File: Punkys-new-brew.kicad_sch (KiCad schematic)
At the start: 64 parts, among them J1 +12v, J10 VCA-CV, J11 1x10_main, J12 1x10_control, J13 L_1x12_main, J14 L_1x12_control, J15 R_1x12_control, J16 R_1x12_main, J17 ScrewHole, J18 ScrewHole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

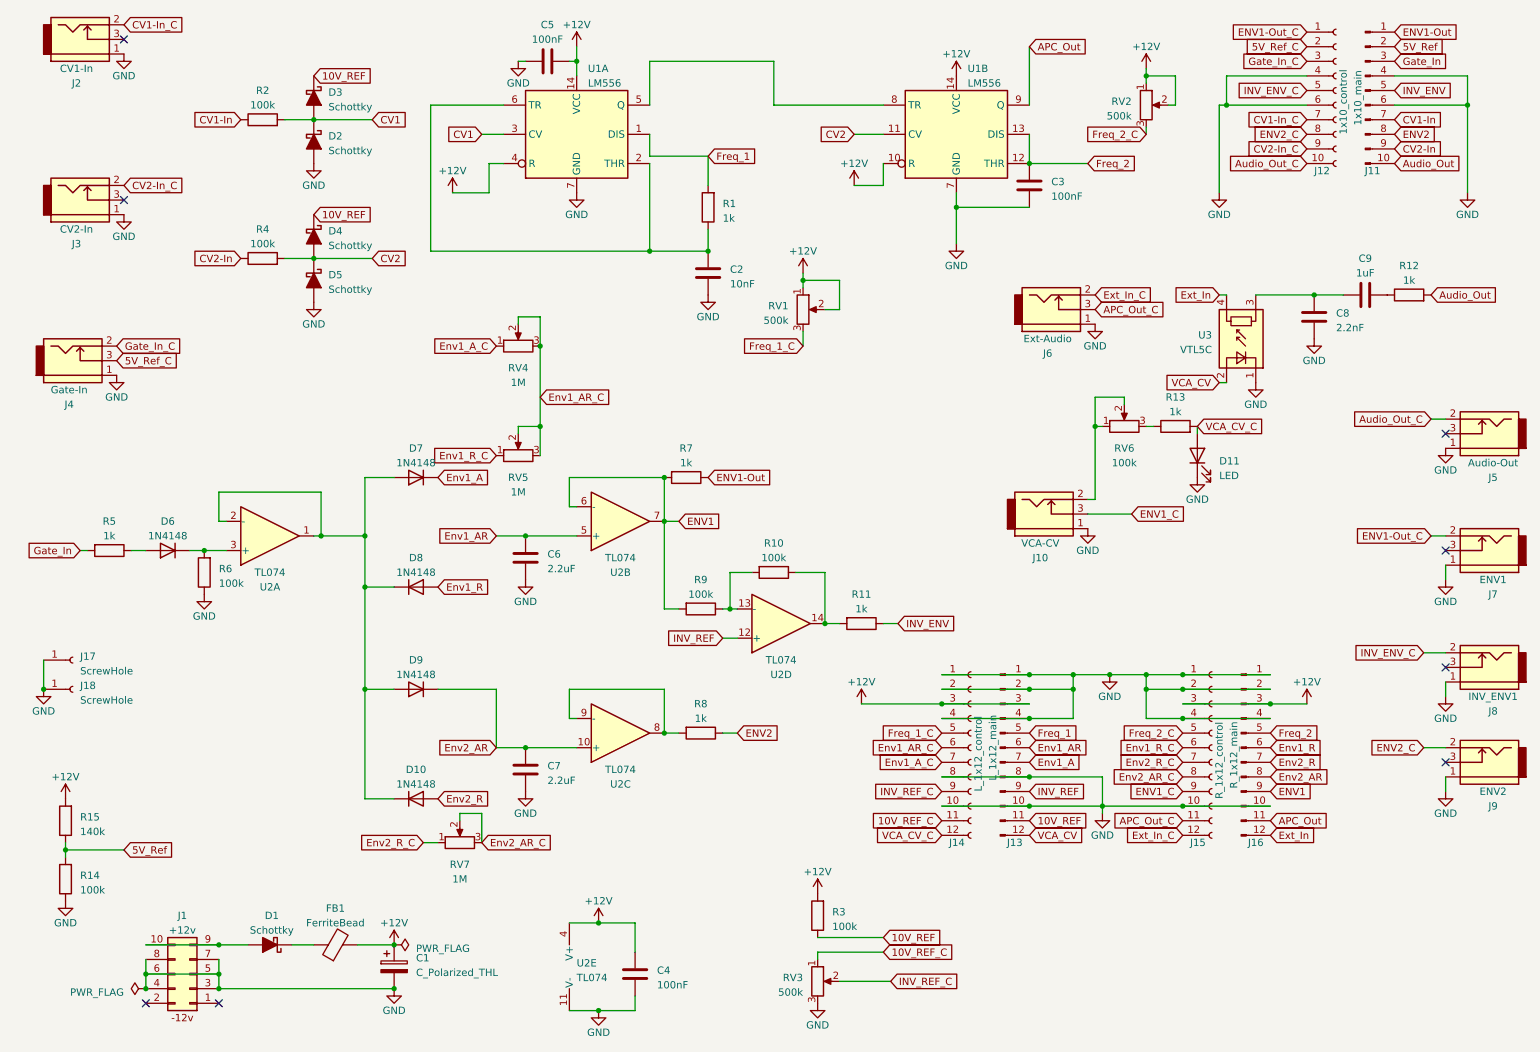
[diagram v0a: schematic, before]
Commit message: fixed some values to better suit my liking. re-routed the invert to env2 instead, it works better me finks.
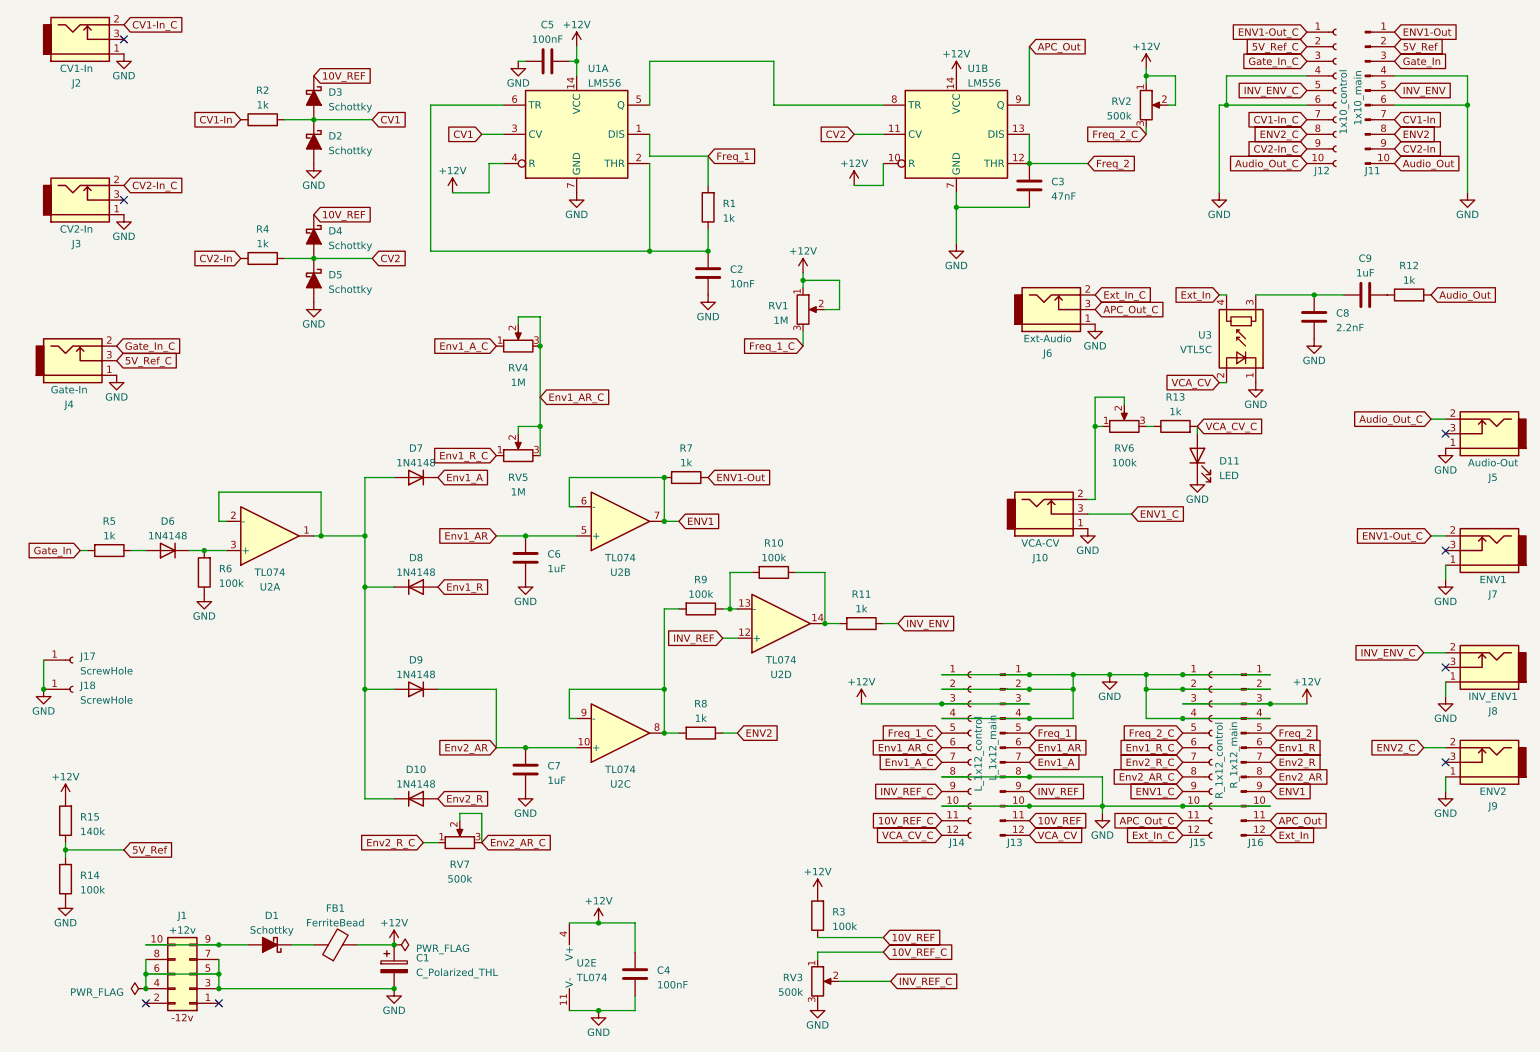
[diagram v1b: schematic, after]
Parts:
- C3: value 100nF -> 47nF
- C6, C7: value 2.2uF -> 1uF
- R2, R4: value 100k -> 1k
- RV1: value 500k -> 1M
- RV7: value 1M -> 500k
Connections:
- net ENV1: no longer R9.2
- net at R8.2, U2.8, U2.9 (-): now also R9.2
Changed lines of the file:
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@@
     (title "Punky's New Brew")
     (date "2023-10-18")
-    (rev "001")
+    (rev "003")
     (company "Scruffy Cat Studios")
   )
@@
   (junction (at 20.32 161.29) (diameter 0) (color 0 0 0 0)
   )
+  (junction (at 124.46 133.35) (diameter 0) (color 0 0 0 0)
+  )
   (junction (at 63.5 58.42) (diameter 0) (color 0 0 0 0)
   )
@@
     (stroke (width 0) (type default))
   )
+  (wire (pts (xy 124.46 119.38) (xy 124.46 133.35))
+    (stroke (width 0) (type default))
+  )
   (wire (pts (xy 256.54 127) (xy 260.35 127))
     (stroke (width 0) (type default))
@@
     (stroke (width 0) (type default))
   )
-  (wire (pts (xy 124.46 119.38) (xy 124.46 104.14))
-    (stroke (width 0) (type default))
-  )
   (wire (pts (xy 132.08 45.72) (xy 132.08 40.64))
     (stroke (width 0) (type default))
@@
       (effects (font (size 1.27 1.27)) (justify right))
     )
-    (property "Value" "500k" (at 146.05 69.215 0)
+    (property "Value" "1M" (at 146.05 69.215 0)
       (effects (font (size 1.27 1.27)) (justify right))
     )
@@
       (effects (font (size 1.27 1.27)))
     )
-    (property "Value" "100k" (at 54.61 31.75 90)
+    (property "Value" "1k" (at 54.61 31.75 90)
       (effects (font (size 1.27 1.27)))
     )
@@
       (effects (font (size 1.27 1.27)) (justify left))
     )
-    (property "Value" "2.2uF" (at 104.14 149.225 0)
+    (property "Value" "1uF" (at 104.14 149.225 0)
       (effects (font (size 1.27 1.27)) (justify left))
     )
@@
       (effects (font (size 1.27 1.27)) (justify left))
     )
-    (property "Value" "100nF" (at 191.77 47.625 0)
+    (property "Value" "47nF" (at 191.77 47.625 0)
       (effects (font (size 1.27 1.27)) (justify left))
     )
@@
       (effects (font (size 1.27 1.27)))
     )
-    (property "Value" "100k" (at 54.61 55.88 90)
+    (property "Value" "1k" (at 54.61 55.88 90)
       (effects (font (size 1.27 1.27)))
     )
@@
       (effects (font (size 1.27 1.27)))
     )
-    (property "Value" "1M" (at 88.9 166.37 90)
+    (property "Value" "500k" (at 88.9 166.37 90)
       (effects (font (size 1.27 1.27)))
     )
@@
       (effects (font (size 1.27 1.27)) (justify left))
     )
-    (property "Value" "2.2uF" (at 104.14 112.395 0)
+    (property "Value" "1uF" (at 104.14 112.395 0)
       (effects (font (size 1.27 1.27)) (justify left))
     )
